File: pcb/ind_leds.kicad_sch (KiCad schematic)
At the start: 6 parts

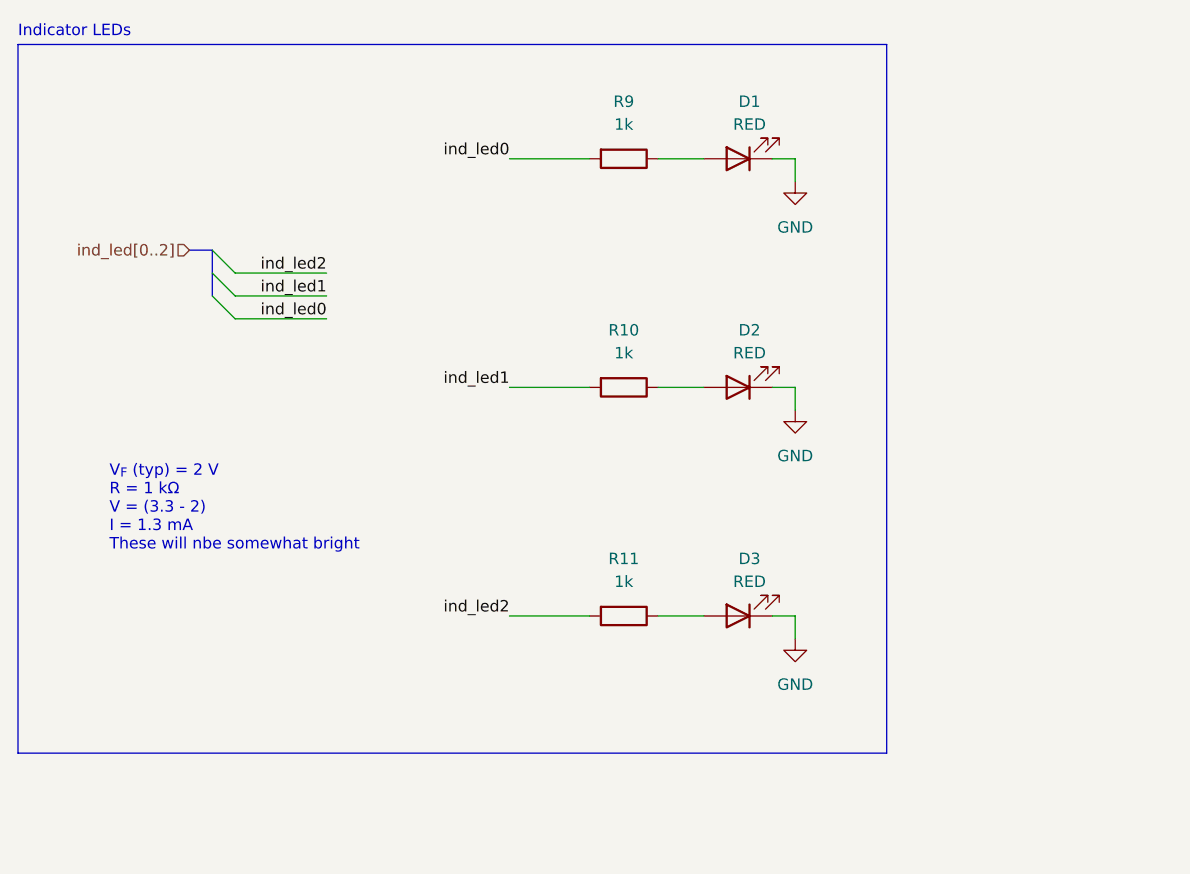
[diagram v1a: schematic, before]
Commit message: custom symbols for all ics
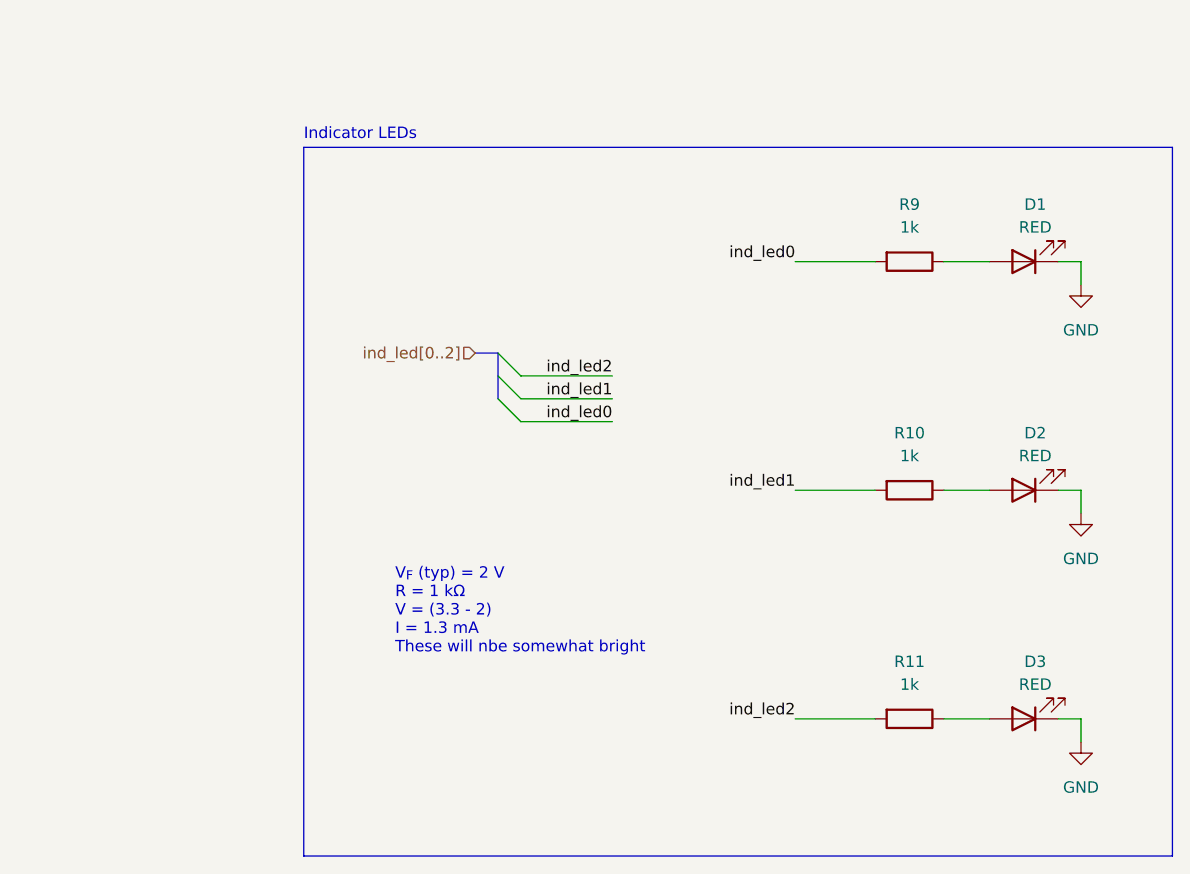
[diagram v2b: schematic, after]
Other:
- moved on the sheet: D1, D2, D3, R10, R11, R9
